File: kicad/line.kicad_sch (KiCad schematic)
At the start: 40 parts, among them J11 AudioJack3, J2 AudioJack3, U12 NE5532, U13 NE5532, U14 NE5532, U15 NE5532

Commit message: tac5212 initial architecture
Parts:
- removed C39, C40: C_Polarized_US, symbol Device:C_Polarized_US
- removed C39, C41, C42, C45: 10uF, symbol Device:C_Polarized_US
- removed C40, C43, C44, C46: 100pF, symbol Device:C
- removed C41, C42, C47, C48: 100uF, symbol Device:C
- removed R75 (x2): 47k, symbol Device:R_US
- removed R76 (x2), R77 (x2), R78 (x2), R79 (x2): 1k, symbol Device:R_US
- removed R80 (x2), R81 (x2): 22k, symbol Device:R_US
- removed R82 (x2), R83 (x2): 68R, symbol Device:R_US
- removed RV4: 2k, symbol openmic:R_Potentiometer_US_Dual
- removed U12, U13, U14, U15: NE5532, symbol Amplifier_Operational:NE5532
- added C95, C96: 100uF, symbol Device:C_Small
- added R53, R54: 100, symbol Device:R_Small_US
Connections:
- new net: C95.1, R53.2
- new net: C96.1, R54.2
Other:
- note removed: "Baxandall amp Gain: -inf to 0dB"

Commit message: line out
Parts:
- removed C95, C96: 100uF, symbol Device:C_Small
- removed J11, J2: AudioJack3, symbol Connector_Audio:AudioJack3
- removed R53, R54: 100, symbol Device:R_Small_US
- added C173: 100uF, symbol Device:C_Polarized_US
- added C174, C175, C176, C177, C178, C179, C180, C181, C182, C184, C186, C187: 100nF, symbol Device:C_Small
- added C183, C185: 0.01uF, symbol Device:C
- added C188: 100uF, symbol Device:C
- added C96: 100nF, symbol Device:C
- added D61, D62, D63, D64, D65, D66, D67, D68, D69, D70, D71, D72: WS2812B-2020, LED_SMD:LED_WS2812B-2020_PLCC4_2.0x2.0mm, symbol LED:WS2812B-2020
- added J2: AudioJack3_Switch, symbol Connector_Audio:AudioJack3_Switch
- added Q1: 2N7002, Package_TO_SOT_SMD:SOT-23, symbol Transistor_FET:2N7002
- added R54: 510, symbol Device:R_US
- added R82, R83, R84, R85: 10k, symbol Device:R_US
- added R86: 100, symbol Device:R_US
- added R87, R88, R89, R90: R, symbol Device:R_US
- added R91: 47k, symbol Device:R_US
- added SW15: RotaryEncoder, symbol Device:RotaryEncoder
- added U14: OPA1637, DGK0008A_N, symbol openmic:OPA1637
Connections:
- net GNDA: now also J2.S, Q1.2 (S), R88.1
- new net: C96.1, J2.SN
- new net: D69.1 (DOUT), D70.3 (DIN)
- new net: D68.1 (DOUT), D69.3 (DIN)
- new net: D67.1 (DOUT), D68.3 (DIN)
- new net: D66.1 (DOUT), D67.3 (DIN)
- new net: J2.T, R90.1, U14.4 (VOUT+)
- new net: R54.1, R88.2, R90.2, U14.1 (VIN-)
- new net: D71.1 (DOUT), D72.3 (DIN)
- new net: D70.1 (DOUT), D71.3 (DIN)
- new net: C183.1, R82.2, R83.1, SW15.A
- new net: C185.1, R84.2, R85.1, SW15.B
- new net: R54.2, R87.2, R89.1, U14.8 (VIN+)
- new net: J2.R, R89.2, U14.5 (VOUT-)
- new net: D65.1 (DOUT), D66.3 (DIN)
- new net: D64.1 (DOUT), D65.3 (DIN)
- new net: Q1.3 (D), U14.7 (PD_N)
- new net: D61.1 (DOUT), D62.3 (DIN)
- new net: D63.1 (DOUT), D64.3 (DIN)
- new net: D62.1 (DOUT), D63.3 (DIN)
- new net: C188.1, R86.2
- new net: C188.2, R87.1
- new net +15V: U14.3 (VS+)
- new net +3V3: R83.2, R84.1, R91.1
- new net +5V: C173.1, C174.1, C175.1, C176.1, C177.1, C178.1, C179.1, C180.1, C181.1, C182.1, C184.1, C186.1, C187.1, D61.4 (VDD), D62.4 (VDD), D63.4 (VDD), D64.4 (VDD), D65.4 (VDD), D66.4 (VDD), D67.4 (VDD), D68.4 (VDD), D69.4 (VDD), D70.4 (VDD), D71.4 (VDD), D72.4 (VDD)
- new net -15V: U14.6 (VS-)
- new net GNDD: C173.2, C174.2, C175.2, C176.2, C177.2, C178.2, C179.2, C180.2, C181.2, C182.2, C183.2, C184.2, C185.2, C186.2, C187.2, D61.2 (VSS), D62.2 (VSS), D63.2 (VSS), D64.2 (VSS), D65.2 (VSS), D66.2 (VSS), D67.2 (VSS), D68.2 (VSS), D69.2 (VSS), D70.2 (VSS), D71.2 (VSS), D72.2 (VSS), SW15.C
- new net IN_L: R86.1
- new net LED_DIN: D61.3 (DIN)
- new net LED_DOUT: D72.1 (DOUT)
- new net LINE_EN_L: Q1.1 (G)
- new net LINE_IND_L: C96.2, R91.2
- new net ROT_A: R82.1
- new net ROT_B: R85.2
- new net V_BIAS: U14.2 (VOCM)

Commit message: line out
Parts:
- added C40: 100uF, symbol Device:C
- added C41: 100nF, symbol Device:C
- added J1: AudioJack3_Switch, symbol Connector_Audio:AudioJack3_Switch
- added Q4: 2N7002, Package_TO_SOT_SMD:SOT-23, symbol Transistor_FET:2N7002
- added R112: 316, symbol Device:R_US
- added R113, R114: 2k, symbol Device:R_US
- added R115: 47k, symbol Device:R_US
- added R93: 215, symbol Device:R_US
- added U15: OPA1637, DGK0008A_N, symbol openmic:OPA1637
- R54: value 510 -> 100
- R87: value R -> 215
- R88: value R -> 316
- R89, R90: value R -> 2k
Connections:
- net V_BIAS is gone; now on net GNDA: U14.2 (VOCM)
- net +15V: now also U15.3 (VS+)
- net +3V3: now also R115.1
- net -15V: now also U15.6 (VS-)
- net GNDA: now also J1.S, Q4.2 (S), R112.1, U15.2 (VOCM)
- net IN_R: now also R54.1
- net at R88.2, R90.2, U14.1 (VIN-): no longer R54.1
- net at R87.2, R89.1, U14.8 (VIN+): no longer R54.2
- new net: J1.R, R113.2, U15.5 (VOUT-)
- new net: C41.1, J1.SN
- new net: J1.T, R114.1, U15.4 (VOUT+)
- new net: R112.2, R114.2, U15.1 (VIN-)
- new net: Q4.3 (D), U15.7 (PD_N)
- new net: R113.1, R93.2, U15.8 (VIN+)
- new net: C40.1, R54.2
- new net: C40.2, R93.1
- new net LINE_EN_R: Q4.1 (G)
- new net LINE_IND_R: C41.2, R115.2
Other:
- moved on the sheet: C188, C96, J2, Q1, R86, R87, R88, R89, R90, R91, U14

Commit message: CH224K external supply
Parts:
- renumbered C188 to C100, C96 to C101, C183 to C102, C185 to C103, C40 to C104, C41 to C105, C173 to C87, C174 to C88, C175 to C89, C176 to C90, C177 to C91, C178 to C92, C179 to C93, C180 to C94, C181 to C95, C182 to C96, C184 to C97, C186 to C98, C187 to C99, D61 to D35, D62 to D36, D63 to D37, D64 to D38, D65 to D39, D66 to D40, D67 to D41, D68 to D42, D69 to D43, D70 to D44, D71 to D45, D72 to D46, J2 to J3, J1 to J4, Q1 to Q3, R91 to R61, R86 to R62, R87 to R63, R89 to R64, R83 to R65, R84 to R66, R82 to R67, R85 to R68, R88 to R69, R90 to R70, R115 to R71, R54 to R72, R93 to R73, R113 to R74, R112 to R75, R114 to R76, SW15 to SW12, U14 to U12, U15 to U13

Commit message: bypass caps
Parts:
- added C193, C194, C195, C196: 100nF, symbol Device:C
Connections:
- net +15V: now also C193.1, C195.1
- net -15V: now also C194.1, C196.1
- net GNDA: now also C193.2, C194.2, C195.2, C196.2
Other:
- moved on the sheet: C101, C105, J3, J4, R61, R71

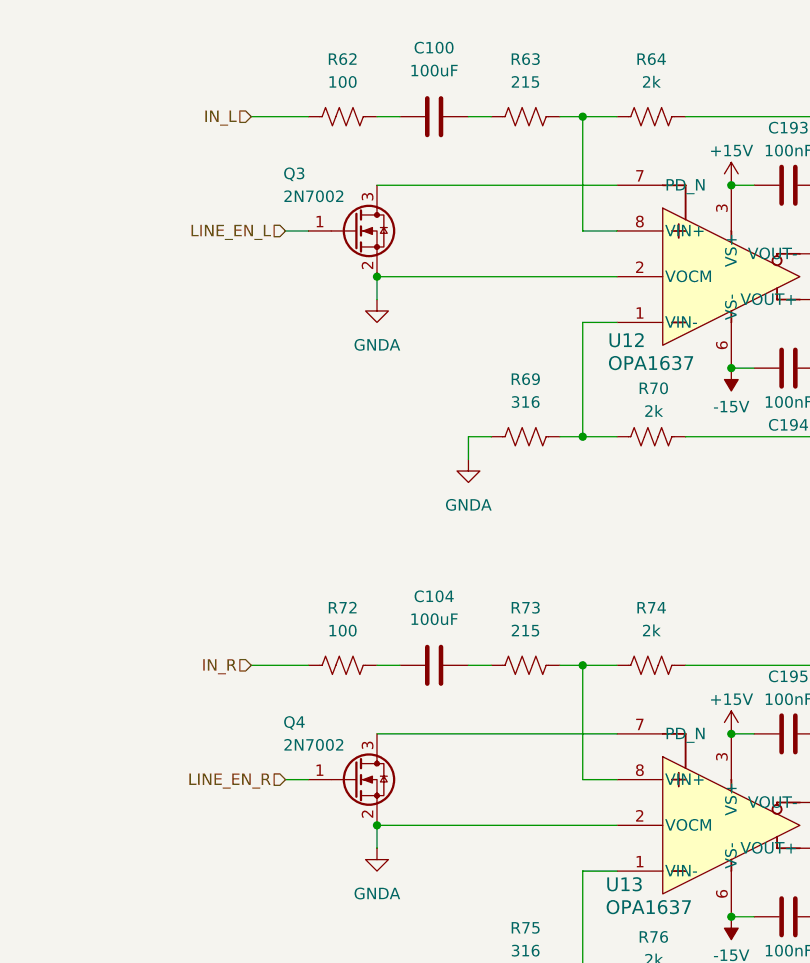
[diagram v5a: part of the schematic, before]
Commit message: replace 2N7002 with CSD13380F3
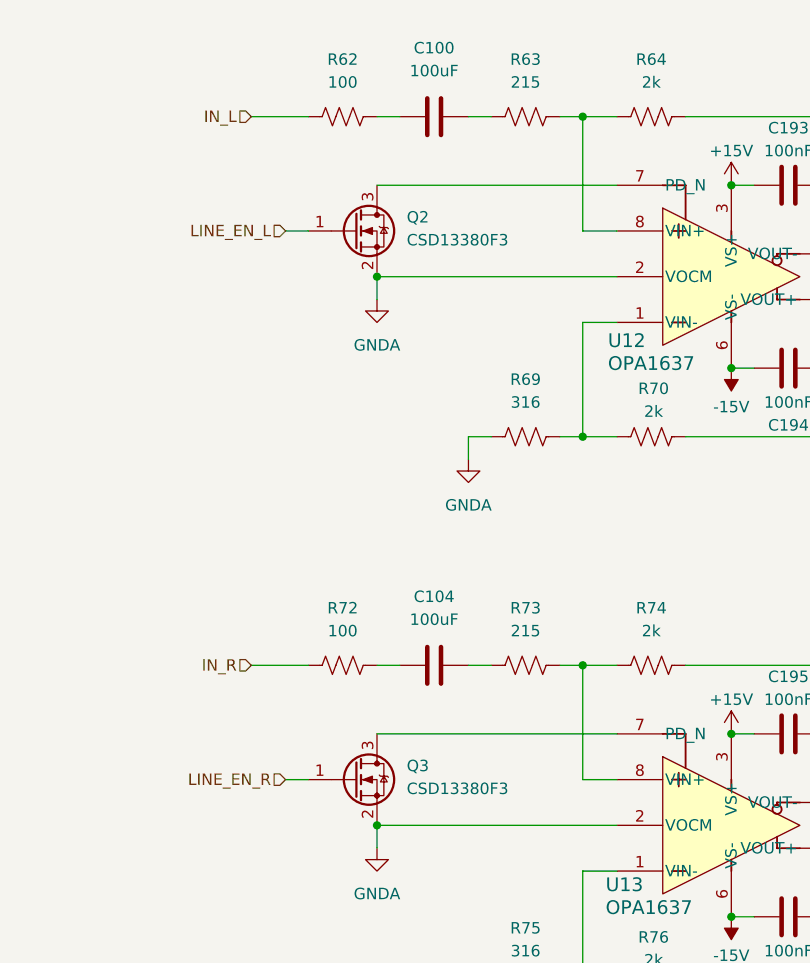
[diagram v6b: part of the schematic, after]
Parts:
- removed Q3, Q4: 2N7002, Package_TO_SOT_SMD:SOT-23, symbol Transistor_FET:2N7002
- added Q2, Q3: CSD13380F3, Package_DFN_QFN:Texas_PicoStar_DFN-3_0.69x0.60mm, symbol Transistor_FET:CSD13380F3
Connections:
- net GNDA: now also Q2.2 (S), Q3.2 (S)
- net LINE_EN_L: now also Q2.1 (G)
- net LINE_EN_R: now also Q3.1 (G)
- net at U13.7 (PD_N): now also Q3.3 (D)
- net at U12.7 (PD_N): now also Q2.3 (D)
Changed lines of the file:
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@@
 	)
 	(junction
+		(at 57.15 95.25)
+		(diameter 0)
+		(color 0 0 0 0)
+	)
+	(junction
 		(at 240.03 104.14)
 		(diameter 0)
@@
 	)
 	(junction
-		(at 57.15 95.25)
-		(diameter 0)
-		(color 0 0 0 0)
-	)
-	(junction
 		(at 229.87 116.84)
 		(diameter 0)
@@
 	)
 	(junction
+		(at 57.15 156.21)
+		(diameter 0)
+		(color 0 0 0 0)
+	)
+	(junction
 		(at 223.52 26.67)
 		(diameter 0)
@@
 	)
 	(junction
-		(at 57.15 156.21)
-		(diameter 0)
-		(color 0 0 0 0)
-	)
-	(junction
 		(at 233.68 26.67)
 		(diameter 0)
@@
 	)
 	(symbol
-		(lib_id "Transistor_FET:2N7002")
+		(lib_id "Transistor_FET:CSD13380F3")
 		(at 54.61 90.17 0)
 		(unit 1)
@@
 		(on_board yes)
 		(dnp no)
-		(property "Reference" "Q3"
-			(at 46.736 83.82 0)
+		(property "Reference" "Q2"
+			(at 60.452 88.646 0)
 			(effects
 				(font
@@
 			)
 		)
-		(property "Value" "2N7002"
-			(at 46.736 86.36 0)
+		(property "Value" "CSD13380F3"
+			(at 60.452 91.186 0)
 			(effects
 				(font
@@
 			)
 		)
-		(property "Footprint" "Package_TO_SOT_SMD:SOT-23"
+		(property "Footprint" "Package_DFN_QFN:Texas_PicoStar_DFN-3_0.69x0.60mm"
 			(at 59.69 92.075 0)
 			(effects
@@
 			)
 		)
-		(property "Datasheet" "https://www.onsemi.com/pub/Collateral/NDS7002A-D.PDF"
+		(property "Datasheet" "https://www.ti.com/lit/ds/symlink/csd13380f3.pdf"
 			(at 59.69 93.98 0)
 			(effects
@@
 			)
 		)
-		(property "Description" "0.115A Id, 60V Vds, N-Channel MOSFET, SOT-23"
-			(at 54.61 90.17 0)
+		(property "Description" "3.6A Id, 12V Vds, N-Channel MOSFET, 76mOhm Ron,max @ 4.5Vgs, 0.91nC Qg,typ @ 4.5Vgs, PicoStar 0.73x0.64mm max, 0.69x0.60mm nom"
+			(at 102.87 90.17 0)
 			(effects
 				(font
@@
 			)
 		)
-		(pin "1"
+		(pin "2"
 		)
 		(pin "3"
 		)
-		(pin "2"
+		(pin "1"
 		)
 		(instances
 			(project "openmic"
 				(path "/84faeadc-8b12-4a66-a17f-5c56e5923fb8/7a7e9668-71cc-4187-873e-ab8d61f232c2"
-					(reference "Q3")
+					(reference "Q2")
 					(unit 1)
 				)
@@
 	)
 	(symbol
+		(lib_id "Transistor_FET:CSD13380F3")
+		(at 54.61 151.13 0)
+		(unit 1)
+		(exclude_from_sim no)
+		(in_bom yes)
+		(on_board yes)
+		(dnp no)
+		(property "Reference" "Q3"
+			(at 60.452 149.606 0)
+			(effects
+				(font
+					(size 1.27 1.27)
+				)
+				(justify left)
+			)
+		)
+		(property "Value" "CSD13380F3"
+			(at 60.452 152.146 0)
+			(effects
+				(font
+					(size 1.27 1.27)
+				)
+				(justify left)
+			)
+		)
+		(property "Footprint" "Package_DFN_QFN:Texas_PicoStar_DFN-3_0.69x0.60mm"
+			(at 59.69 153.035 0)
+			(effects
+				(font
+					(size 1.27 1.27)
+					(italic yes)
+				)
+				(justify left)
+				(hide yes)
+			)
+		)
+		(property "Datasheet" "https://www.ti.com/lit/ds/symlink/csd13380f3.pdf"
+			(at 59.69 154.94 0)
+			(effects
+				(font
+					(size 1.27 1.27)
+				)
+				(justify left)
+				(hide yes)
+			)
+		)
+		(property "Description" "3.6A Id, 12V Vds, N-Channel MOSFET, 76mOhm Ron,max @ 4.5Vgs, 0.91nC Qg,typ @ 4.5Vgs, PicoStar 0.73x0.64mm max, 0.69x0.60mm nom"
+			(at 102.87 151.13 0)
+			(effects
+				(font
+					(size 1.27 1.27)
+				)
+				(hide yes)
+			)
+		)
+		(pin "2"
+		)
+		(pin "3"
+		)
+		(pin "1"
+		)
+		(instances
+			(project "openmic"
+				(path "/84faeadc-8b12-4a66-a17f-5c56e5923fb8/7a7e9668-71cc-4187-873e-ab8d61f232c2"
+					(reference "Q3")
+					(unit 1)
+				)
+			)
+		)
+	)
+	(symbol
 		(lib_id "Connector_Audio:AudioJack3_Switch")
 		(at 129.54 92.71 0)
@@
 					(unit 1)
 				)
-			)
-		)
-	)
-	(symbol
-		(lib_id "Transistor_FET:2N7002")
-		(at 54.61 151.13 0)
-		(unit 1)
-		(exclude_from_sim no)
-		(in_bom yes)
-		(on_board yes)
-		(dnp no)
-		(property "Reference" "Q4"
-			(at 46.736 144.78 0)
-			(effects
-				(font
-					(size 1.27 1.27)
-				)
-				(justify left)
-			)
-		)
-		(property "Value" "2N7002"
-			(at 46.736 147.32 0)
-			(effects
-				(font
-					(size 1.27 1.27)
-				)
-				(justify left)
-			)
-		)
-		(property "Footprint" "Package_TO_SOT_SMD:SOT-23"
-			(at 59.69 153.035 0)
-			(effects
-				(font
-					(size 1.27 1.27)
-					(italic yes)
-				)
-				(justify left)
-				(hide yes)
-			)
-		)
-		(property "Datasheet" "https://www.onsemi.com/pub/Collateral/NDS7002A-D.PDF"
-			(at 59.69 154.94 0)
-			(effects
-				(font
-					(size 1.27 1.27)
-				)
-				(justify left)
-				(hide yes)
-			)
-		)
-		(property "Description" "0.115A Id, 60V Vds, N-Channel MOSFET, SOT-23"
-			(at 54.61 151.13 0)
-			(effects
-				(font
-					(size 1.27 1.27)
-				)
-				(hide yes)
-			)
-		)
-		(pin "1"
-		)
-		(pin "3"
-		)
-		(pin "2"
-		)
-		(instances
-			(project "openmic"
-				(path "/84faeadc-8b12-4a66-a17f-5c56e5923fb8/7a7e9668-71cc-4187-873e-ab8d61f232c2"
-					(reference "Q4")
-					(unit 1)
-				)
